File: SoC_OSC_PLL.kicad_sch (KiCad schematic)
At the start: 3 parts

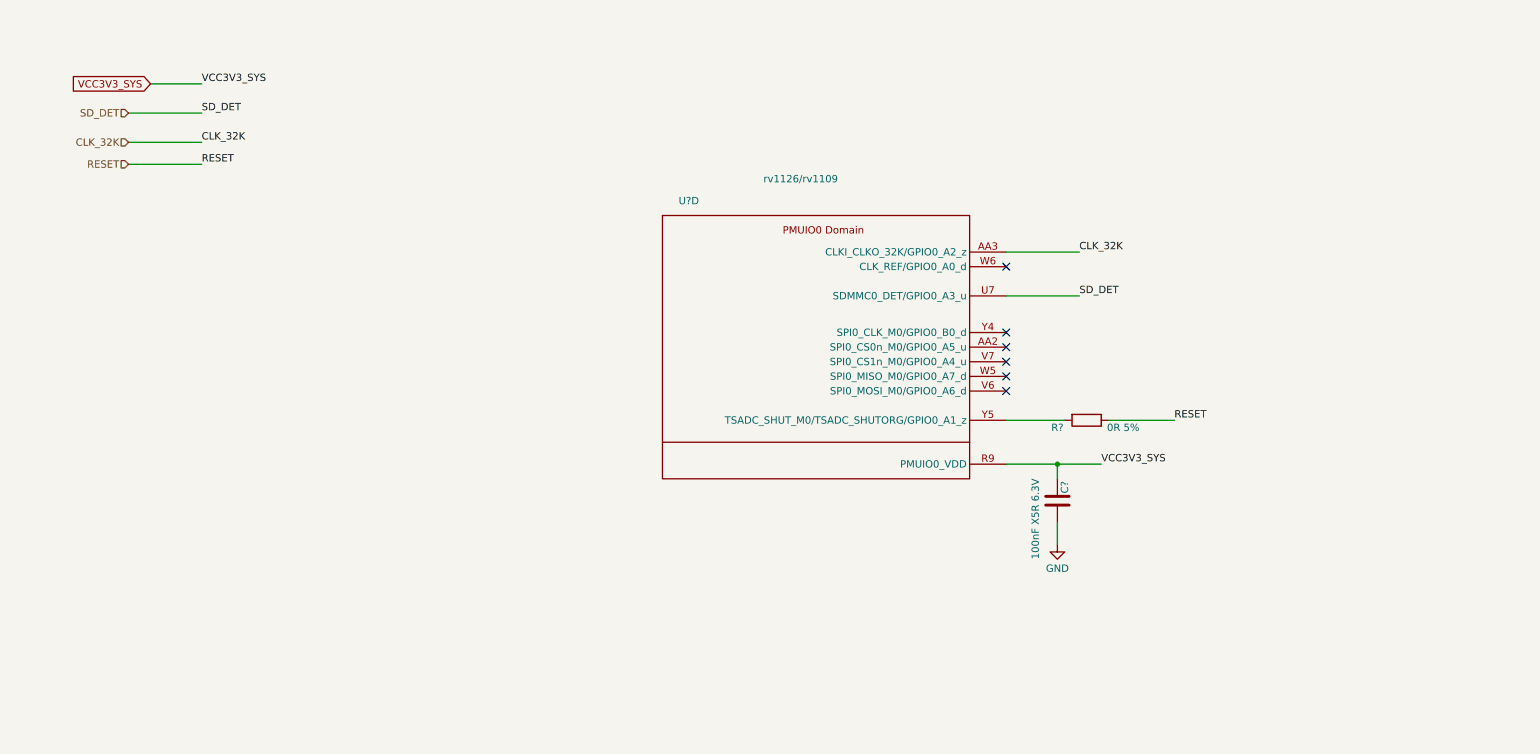
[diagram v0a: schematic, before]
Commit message: added OSC, updated annotations
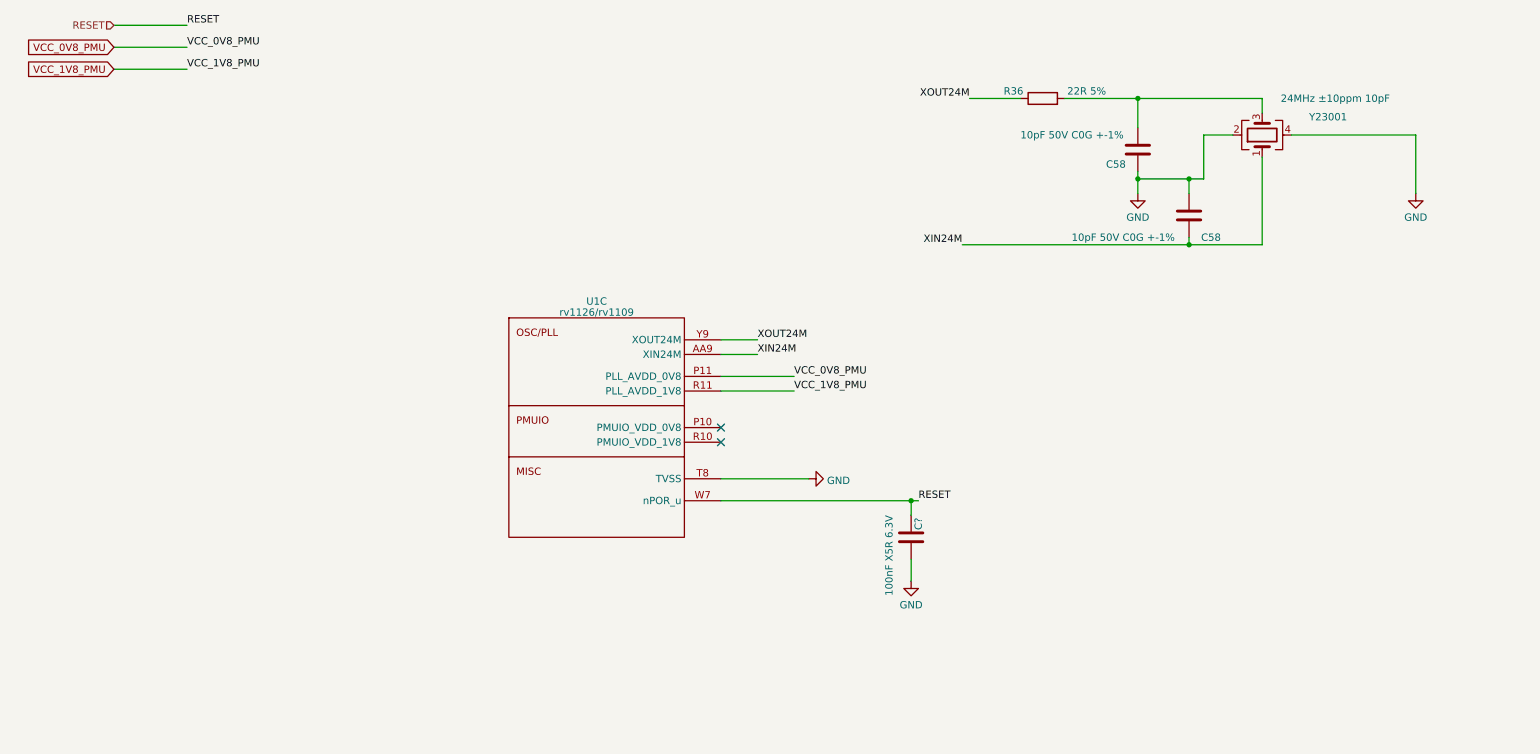
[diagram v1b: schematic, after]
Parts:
- removed C?: 100nF X5R 6.3V, Capacitor_SMD:C_0201_0603Metric, symbol Device:C
- removed R?: 0R 5%, Resistor_SMD:R_0402_1005Metric, symbol Device:R
- removed U?: rv1126/rv1109, Rockchip_SoC:Rockchip_RV1126_FCCSP409LD_14.0x14.0mm, symbol CPU_Rockchip:rv1126_rv1109
- added C58 (x2): 10pF 50V C0G +-1%, Capacitor_SMD:C_0402_1005Metric, symbol Device:C
- added C?: 100nF X5R 6.3V, Capacitor_SMD:C_0201_0603Metric, symbol Device:C
- added R36: 22R 5%, Resistor_SMD:R_0402_1005Metric, symbol Device:R
- added U1: rv1126/rv1109, Rockchip_SoC:Rockchip_RV1126_FCCSP409LD_14.0x14.0mm, symbol CPU_Rockchip:rv1126_rv1109
- added Y23001: 24MHz ±10ppm 10pF, Crystal:Crystal_SMD_2520-4Pin_2.5x2.0mm, symbol Device:Crystal_GND24
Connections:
- net GND: now also C58.1, C58.1, C?.2, U1.T8 (TVSS), Y23001.2, Y23001.4
- net RESET: now also C?.1, U1.W7 (nPOR_u)
- new net: C58.2, R36.2, Y23001.3
- new net VCC_0V8_PMU: U1.P11 (PLL_AVDD_0V8)
- new net VCC_1V8_PMU: U1.R11 (PLL_AVDD_1V8)
- new net XIN24M: C58.2, U1.AA9 (XIN24M), Y23001.1
- new net XOUT24M: R36.1, U1.Y9 (XOUT24M)
- no-connect marks 6 -> 2

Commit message: added Decoupling C for PMUIO_0V8/1V8
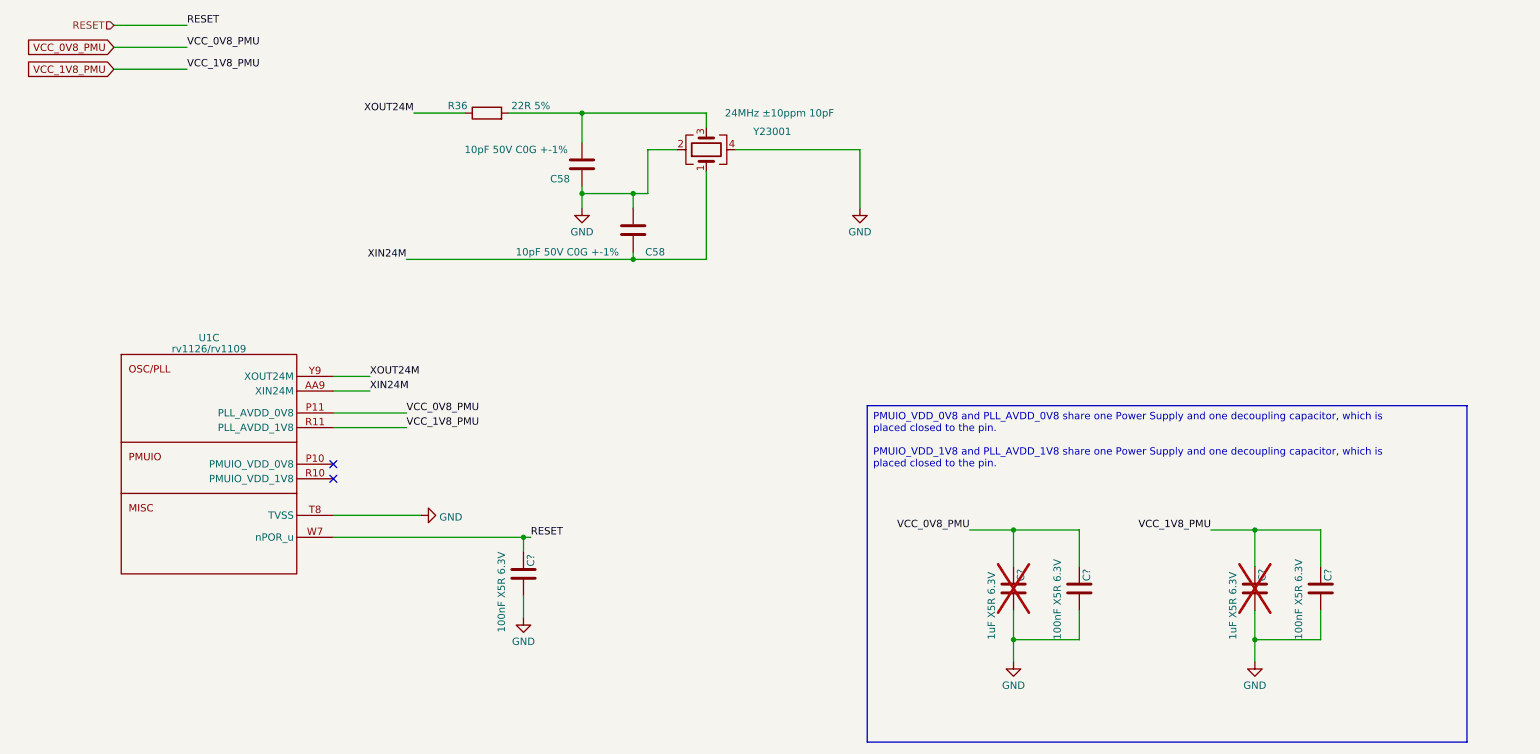
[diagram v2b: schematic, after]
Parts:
- added C? (x2): 1uF X5R 6.3V, Capacitor_SMD:C_0402_1005Metric, symbol Device:C
- added C? (x2): 100nF X5R 6.3V, Capacitor_SMD:C_0201_0603Metric, symbol Device:C
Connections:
- net GND: now also C?.2, C?.2, C?.2, C?.2
- net VCC_0V8_PMU: now also C?.1, C?.1
- net VCC_1V8_PMU: now also C?.1, C?.1
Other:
- moved on the sheet: C58, C?, R36, U1C, Y23001

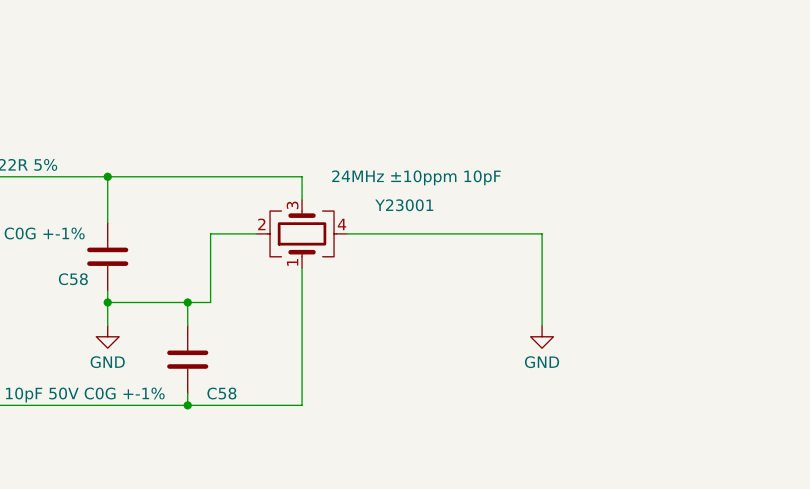
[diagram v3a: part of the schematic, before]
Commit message: move DDR power decoupling capacitors into DDR4 Sheet
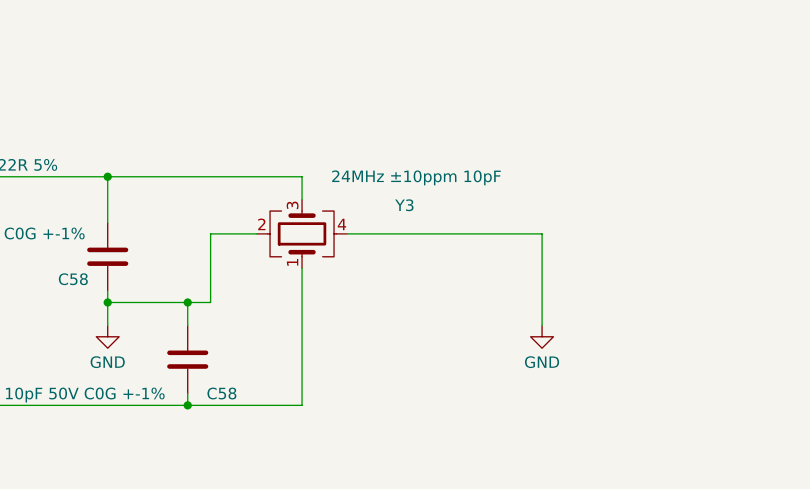
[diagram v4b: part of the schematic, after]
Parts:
- renumbered Y23001 to Y3
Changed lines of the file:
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@@
         )
         (path "/e3b58043-16a3-43c8-9fad-9c9784eebfa4/56cc099e-27f5-4b56-badd-873635da3ec1"
-          (reference "C23004") (unit 1)
+          (reference "C141") (unit 1)
         )
       )
@@
         )
         (path "/e3b58043-16a3-43c8-9fad-9c9784eebfa4/56cc099e-27f5-4b56-badd-873635da3ec1"
-          (reference "C23007") (unit 1)
+          (reference "C144") (unit 1)
         )
       )
@@
         )
         (path "/e3b58043-16a3-43c8-9fad-9c9784eebfa4/56cc099e-27f5-4b56-badd-873635da3ec1"
-          (reference "#PWR023003") (unit 1)
+          (reference "#PWR0123") (unit 1)
         )
       )
@@
         )
         (path "/e3b58043-16a3-43c8-9fad-9c9784eebfa4/56cc099e-27f5-4b56-badd-873635da3ec1"
-          (reference "R23001") (unit 1)
+          (reference "R58") (unit 1)
         )
       )
@@
         )
         (path "/e3b58043-16a3-43c8-9fad-9c9784eebfa4/56cc099e-27f5-4b56-badd-873635da3ec1"
-          (reference "C23001") (unit 1)
+          (reference "C138") (unit 1)
         )
       )
@@
         )
         (path "/e3b58043-16a3-43c8-9fad-9c9784eebfa4/56cc099e-27f5-4b56-badd-873635da3ec1"
-          (reference "#PWR023004") (unit 1)
+          (reference "#PWR0124") (unit 1)
         )
       )
@@
         )
         (path "/e3b58043-16a3-43c8-9fad-9c9784eebfa4/56cc099e-27f5-4b56-badd-873635da3ec1"
-          (reference "C23005") (unit 1)
+          (reference "C142") (unit 1)
         )
       )
@@
         )
         (path "/e3b58043-16a3-43c8-9fad-9c9784eebfa4/56cc099e-27f5-4b56-badd-873635da3ec1"
-          (reference "#PWR023006") (unit 1)
+          (reference "#PWR0126") (unit 1)
         )
       )
@@
         )
         (path "/e3b58043-16a3-43c8-9fad-9c9784eebfa4/56cc099e-27f5-4b56-badd-873635da3ec1"
-          (reference "#PWR023005") (unit 1)
+          (reference "#PWR0125") (unit 1)
         )
       )
@@
   (symbol (lib_id "Device:Crystal_GND24") (at 134.62 44.45 90) (unit 1)
     (in_bom yes) (on_board yes) (dnp no)
-    (property "Reference" "Y23001" (at 146.0609 41.3131 90)
+    (property "Reference" "Y3" (at 146.0609 41.3131 90)
       (effects (font (size 1.27 1.27)))
     )
@@
       (project "leaf"
         (path "/e3b58043-16a3-43c8-9fad-9c9784eebfa4/56cc099e-27f5-4b56-badd-873635da3ec1"
-          (reference "Y23001") (unit 1)
+          (reference "Y3") (unit 1)
         )
       )
@@
         )
         (path "/e3b58043-16a3-43c8-9fad-9c9784eebfa4/56cc099e-27f5-4b56-badd-873635da3ec1"
-          (reference "C23003") (unit 1)
+          (reference "C140") (unit 1)
         )
       )
@@
         )
         (path "/e3b58043-16a3-43c8-9fad-9c9784eebfa4/56cc099e-27f5-4b56-badd-873635da3ec1"
-          (reference "C23006") (unit 1)
+          (reference "C143") (unit 1)
         )
       )
@@
         )
         (path "/e3b58043-16a3-43c8-9fad-9c9784eebfa4/56cc099e-27f5-4b56-badd-873635da3ec1"
-          (reference "C23002") (unit 1)
+          (reference "C139") (unit 1)
         )
       )
@@
         )
         (path "/e3b58043-16a3-43c8-9fad-9c9784eebfa4/56cc099e-27f5-4b56-badd-873635da3ec1"
-          (reference "#PWR023001") (unit 1)
+          (reference "#PWR0121") (unit 1)
         )
       )
@@
         )
         (path "/e3b58043-16a3-43c8-9fad-9c9784eebfa4/56cc099e-27f5-4b56-badd-873635da3ec1"
-          (reference "U3001") (unit 3)
+          (reference "U2") (unit 3)
         )
       )
@@
         )
         (path "/e3b58043-16a3-43c8-9fad-9c9784eebfa4/56cc099e-27f5-4b56-badd-873635da3ec1"
-          (reference "#PWR023002") (unit 1)
-        )
-      )
+          (reference "#PWR0122") (unit 1)
+        )
+      )

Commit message: added README and license
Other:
- company: (none) -> Yang Hongbo
- title: (none) -> Leaf RV1126
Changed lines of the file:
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@@
 (kicad_sch (version 20230121) (generator eeschema)
   (paper "A4")
+  (title_block
+    (title "Leaf RV1126")
+    (date "2023-06-07")
+    (company "Yang Hongbo")
+    (comment 1 "License: CC BY-SA")
+  )
   (junction (at 229.87 129.54) (diameter 0) (color 0 0 0 0)
   )
